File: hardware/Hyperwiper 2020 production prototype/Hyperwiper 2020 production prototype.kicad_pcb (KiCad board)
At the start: 2 copper layers, 87.6 x 59.1 mm, 12 parts, among them K1 Main Power relay, K2 Wiper control relay, Q1 PN2222A, U1 Teensy4.0, U2 Audio board, U3 L7805

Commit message: Updates schematic and PCB boards
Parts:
- added R4: R, Resistor_THT:R_Axial_DIN0207_L6.3mm_D2.5mm_P10.16mm_Horizontal, F.Cu at (972.2, 35.0)
- added R5: R, Resistor_THT:R_Axial_DIN0207_L6.3mm_D2.5mm_P10.16mm_Horizontal, F.Cu at (976.4, 35.0)
- added R6: R, Resistor_THT:R_Axial_DIN0207_L6.3mm_D2.5mm_P10.16mm_Horizontal, F.Cu at (972.2, 48.3)
- added R7: R, Resistor_THT:R_Axial_DIN0207_L6.3mm_D2.5mm_P10.16mm_Horizontal, F.Cu at (976.4, 48.3)
- added R8: R, Resistor_THT:R_Axial_DIN0207_L6.3mm_D2.5mm_P10.16mm_Horizontal, F.Cu at (980.4, 48.3)
- added R9: R, Resistor_THT:R_Axial_DIN0207_L6.3mm_D2.5mm_P10.16mm_Horizontal, F.Cu at (980.4, 35.0)
- moved R1 56.3 mm to (980.4, 11.4), turned to -90 degrees
- moved R2 51.8 mm to (976.4, 21.6), turned to 90 degrees
- moved R3 39.2 mm to (972.2, 21.6), turned to 90 degrees
- moved Q1 18.0 mm to (950.0, 56.5)
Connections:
- D1 pad 1: (no net) -> GND
- D1 pad 2: (no net) -> Net-(D1-Pad2)
- D1 pad 3: (no net) -> Net-(D1-Pad3)
- D1 pad 4: (no net) -> Net-(D1-Pad4)
- D2 pad 1: (no net) -> GND
- D2 pad 2: (no net) -> Net-(D2-Pad2)
- D2 pad 3: (no net) -> Net-(D2-Pad3)
- D2 pad 4: (no net) -> Net-(D2-Pad4)
- D3 pad 1: Net-(D3-Pad1) -> GND
- D3 pad 2: GND -> Net-(D3-Pad2)
- K1 pad 1: (no net) -> Net-(K1-Pad1)
- K2 pad 1: (no net) -> Net-(K1-Pad4)
- K2 pad 3: (no net) -> Net-(K1-Pad1)
- R3 pad 1: Net-(D3-Pad1) -> Net-(D3-Pad2)

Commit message: Update Schematics and PCB
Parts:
- removed R2: R, Resistor_THT:R_Axial_DIN0207_L6.3mm_D2.5mm_P10.16mm_Horizontal
- R1: value R -> 10k
- R3, R4, R5, R6, R7, R8, R9: value R -> 470
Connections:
- R3 pad 2: Net-(K1-Pad3) -> /33

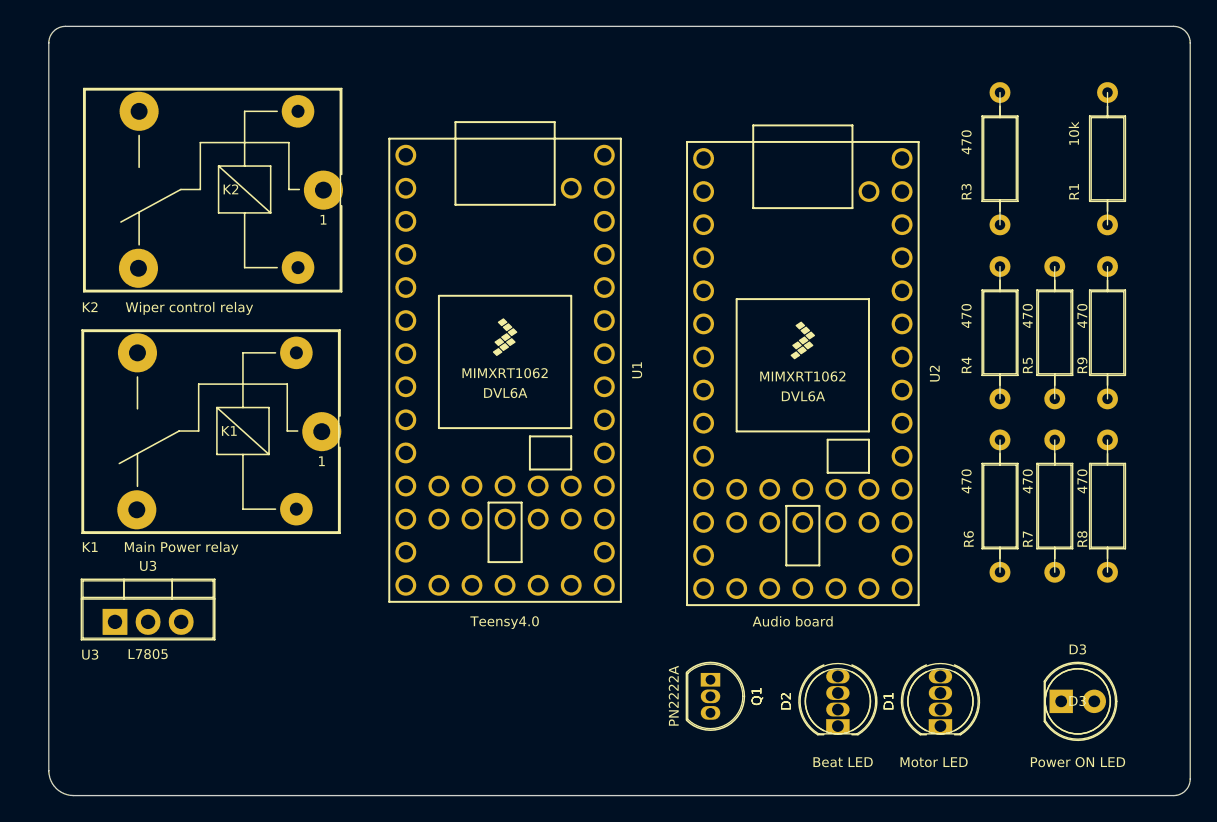
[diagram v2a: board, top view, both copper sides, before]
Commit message: Updated darft schemetics and board.
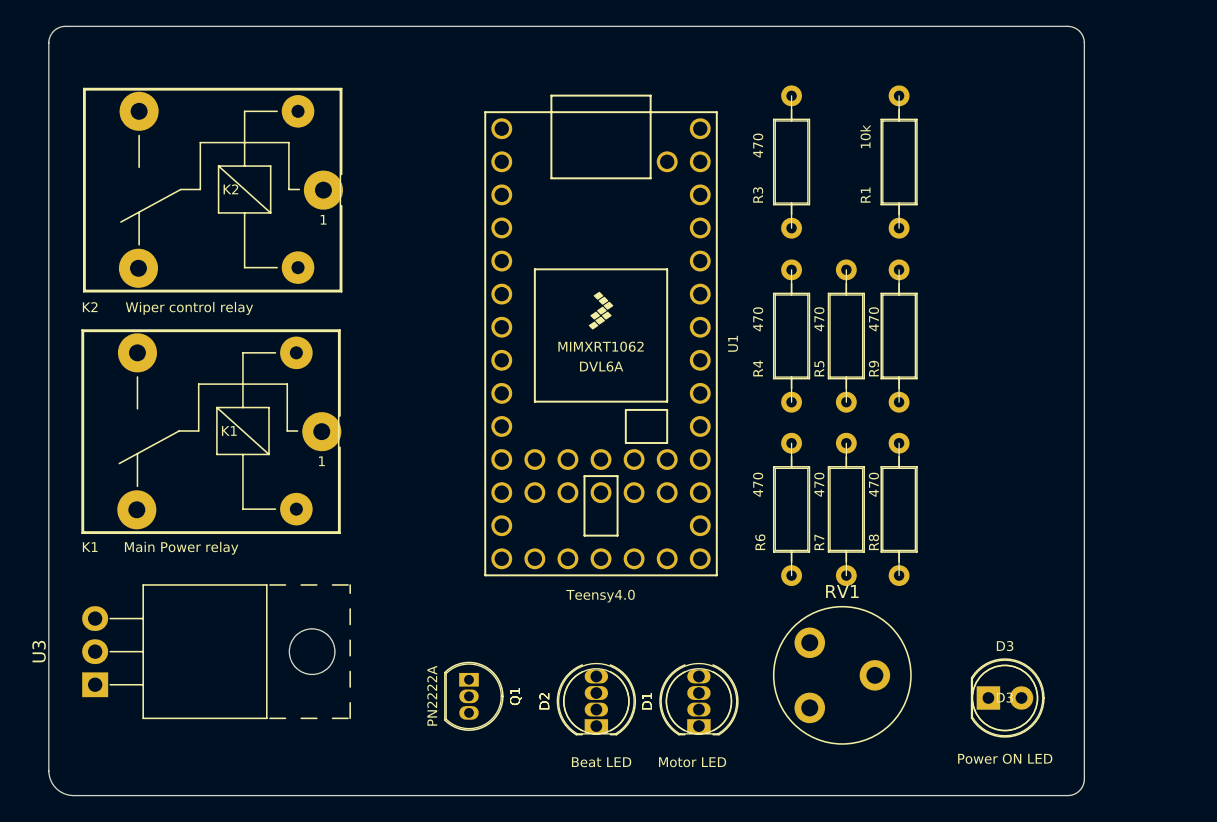
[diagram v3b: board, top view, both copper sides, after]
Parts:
- removed U2: Audio board, Teensy:Teensy40
- added RV1: R_POT_TRIM, Potentiometer_THT:Potentiometer_Piher_PT-10-V05_Vertical, F.Cu at (957.6, 58.7)
- U3: footprint Package_TO_SOT_THT:TO-220-3_Vertical -> Package_TO_SOT_THT:TO-220-3_Horizontal_TabUp
- moved D1 18.5 mm to (949.1, 60.1)
- moved D2 18.5 mm to (941.2, 60.1)
- moved Q1 18.5 mm to (931.4, 56.5)
- moved R1 16.0 mm to (964.4, 11.7)
- moved R8 16.0 mm to (964.4, 48.5)
- moved R9 16.0 mm to (964.4, 35.2)
- moved R3 16.0 mm to (956.2, 21.8)
- moved R4 16.0 mm to (956.2, 35.2)
- moved R5 16.0 mm to (960.4, 35.2)
- moved R6 16.0 mm to (956.2, 48.5)
- moved R7 16.0 mm to (960.4, 48.5)
- moved U1 7.64 mm to (941.6, 30.7)
- moved D3 5.59 mm to (971.3, 57.9)
- moved U3 5.06 mm to (902.7, 56.9), turned to 90 degrees
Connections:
- net /33 renamed /5V
- U1 pad 1: /1 -> (no net)
- U1 pad 10: /10 -> (no net)
- U1 pad 11: /11 -> (no net)
- U1 pad 12: /12 -> (no net)
- U1 pad 13: /13 -> (no net)
- U1 pad 14: /14 -> (no net)
- U1 pad 15: /15 -> (no net)
- U1 pad 16: /16 -> (no net)
- U1 pad 17: /17 -> (no net)
- U1 pad 18: /18 -> (no net)
- U1 pad 19: /19 -> (no net)
- U1 pad 2: /2 -> (no net)
- U1 pad 20: /20 -> (no net)
- U1 pad 21: /21 -> (no net)
- U1 pad 22: /22 -> (no net)
- U1 pad 23: /23 -> (no net)
- U1 pad 24: /24 -> (no net)
- U1 pad 25: /25 -> (no net)
- U1 pad 26: /26 -> (no net)
- U1 pad 27: /27 -> (no net)
- U1 pad 28: /28 -> (no net)
- U1 pad 29: /29 -> (no net)
- U1 pad 3: /3 -> (no net)
- U1 pad 30: /30 -> (no net)
- U1 pad 31: /31 -> (no net)
- U1 pad 32: /32 -> GND
- U1 pad 34: /34 -> (no net)
- U1 pad 4: /4 -> (no net)
- U1 pad 5: /5 -> (no net)
- U1 pad 6: /6 -> (no net)
- U1 pad 7: /7 -> (no net)
- U1 pad 8: /8 -> (no net)
- U1 pad 9: /9 -> (no net)
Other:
- board size 87.6 x 59.1 mm -> 79.5 x 59.1 mm

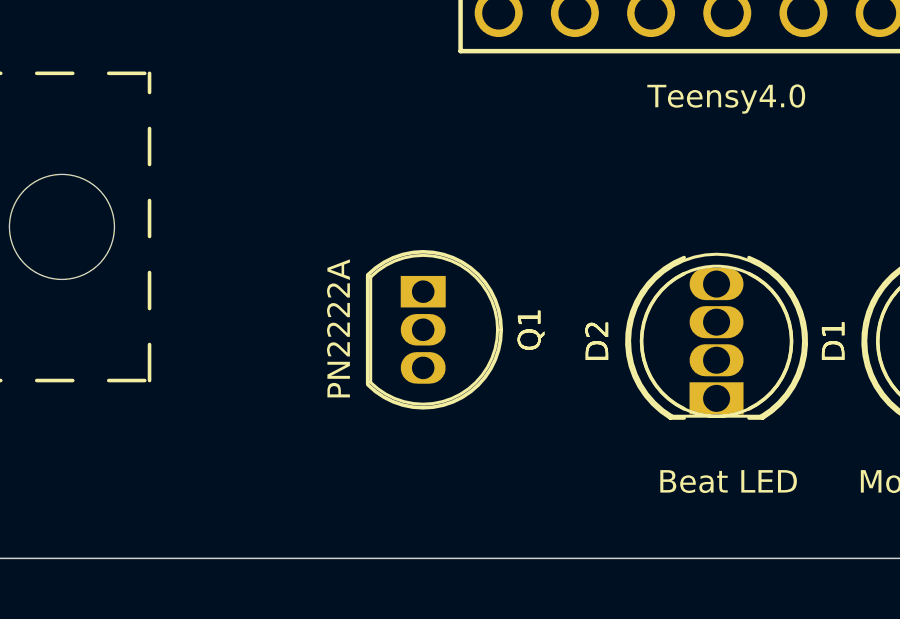
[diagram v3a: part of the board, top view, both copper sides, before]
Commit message: Took out the joystick and display funtions.
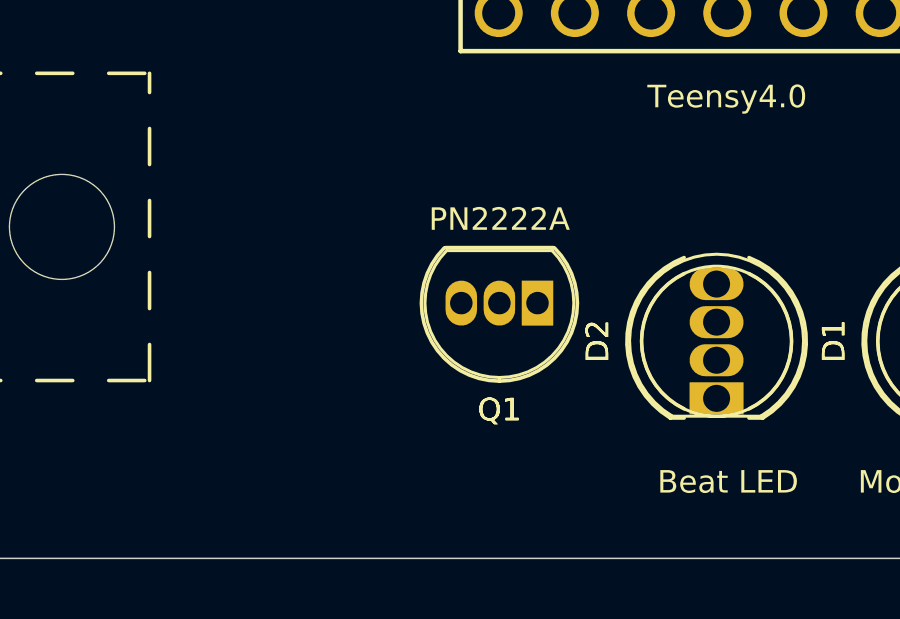
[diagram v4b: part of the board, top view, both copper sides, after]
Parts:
- moved Q1 3.83 mm to (935.2, 56.9), turned to 180 degrees
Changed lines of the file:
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@@
       (net 3 "Net-(K1-Pad3)") (pinfunction "IN"))
     (pad "" np_thru_hole oval (at 2.54 16.66 90) (size 3.5 3.5) (drill 3.5) (layers *.Cu *.Mask))
-    (model "${KISYS3DMOD}/Package_TO_SOT_THT.3dshapes/TO-220-3_Vertical.wrl"
-      (at (xyz 0 0 0))
-      (scale (xyz 1 1 1))
-      (rotate (xyz 0 0 0))
+    (model "${KISYS3DMOD}/Package_TO_SOT_THT.3dshapes/TO-220-3_Horizontal_TabDown.step"
+      (offset (xyz 5 0 0))
+      (scale (xyz 1 1 1))
+      (rotate (xyz 0 0 180))
     )
   )
@@
       (scale (xyz 1 1 1))
       (rotate (xyz 0 0 0))
+    )
+    (model "${KISYS3DMOD}/Potentiometer_THT.3dshapes/Potentiometer_Bourns_3339P_Vertical.step"
+      (offset (xyz 2 5.5 0.5))
+      (scale (xyz 1.2 1.2 1.1))
+      (rotate (xyz 0 0 180))
     )
   )
@@
   )
   (module "Package_TO_SOT_THT:TO-92_Inline" (layer "F.Cu")
-    (at 931.418 56.515 -90)
+    (at 935.228 56.896 180)
     (descr "TO-92 leads in-line, narrow, oval pads, drill 0.75mm (see NXP sot054_po.pdf)")
     (tags "to-92 sc-43 sc-43a sot54 PA33 transistor")
-    (fp_text reference "Q1" (at 1.27 -3.56 90) (layer "F.SilkS")
-      (effects (font (size 0.75 0.75) (thickness 0.15)))
-    )
-    (fp_text value "PN2222A" (at 1.27 2.79 90 unlocked) (layer "F.SilkS")
+    (fp_text reference "Q1" (at 1.27 -3.56) (layer "F.SilkS")
+      (effects (font (size 0.75 0.75) (thickness 0.15)))
+    )
+    (fp_text value "PN2222A" (at 1.27 2.79 unlocked) (layer "F.SilkS")
       (effects (font (size 0.75 0.75) (thickness 0.15)))
     )
@@
     (fp_line (start -0.5 1.75) (end 3 1.75) (layer "F.SilkS") (width 0.1))
     (fp_line (start -0.53 1.85) (end 3.07 1.85) (layer "F.SilkS") (width 0.12))
-    (fp_text user "${REFERENCE}" (at 1.27 -3.56 90 unlocked) (layer "F.SilkS")
-      (effects (font (size 0.75 0.75) (thickness 0.15)))
-    )
-    (pad "1" thru_hole rect (at 0 0 270) (size 1.05 1.5) (drill 0.75) (layers *.Cu *.Mask)
+    (fp_text user "${REFERENCE}" (at 1.27 -3.56 unlocked) (layer "F.SilkS")
+      (effects (font (size 0.75 0.75) (thickness 0.15)))
+    )
+    (pad "1" thru_hole rect (at 0 0 180) (size 1.05 1.5) (drill 0.75) (layers *.Cu *.Mask)
       (net 5 "GND") (pinfunction "E"))
-    (pad "3" thru_hole oval (at 2.54 0 270) (size 1.05 1.5) (drill 0.75) (layers *.Cu *.Mask)
+    (pad "3" thru_hole oval (at 2.54 0 180) (size 1.05 1.5) (drill 0.75) (layers *.Cu *.Mask)
       (net 4 "Net-(K2-Pad2)") (pinfunction "C"))
-    (pad "2" thru_hole oval (at 1.27 0 270) (size 1.05 1.5) (drill 0.75) (layers *.Cu *.Mask)
+    (pad "2" thru_hole oval (at 1.27 0 180) (size 1.05 1.5) (drill 0.75) (layers *.Cu *.Mask)
       (net 6 "Net-(Q1-Pad2)") (pinfunction "B"))
     (model "${KISYS3DMOD}/Package_TO_SOT_THT.3dshapes/TO-92_Inline.wrl"

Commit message: Updated Schematic and board.
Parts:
- added X1: W237-3E-bGeigieNanoKit_V1.1r5a-eagle-import, DWP 2020:W237-3E, F.Cu at (910.3, 55.9)
- added X2: W237-3E-bGeigieNanoKit_V1.1r5a-eagle-import, DWP 2020:W237-3E, F.Cu at (926.7, 55.9)
- U3: footprint Package_TO_SOT_THT:TO-220-3_Horizontal_TabUp -> Package_TO_SOT_THT:TO-220-3_Vertical
- moved U3 20.9 mm to (904.0, 36.1)
- moved R3 20.1 mm to (975.4, 15.9), turned to 180 degrees
- moved U1 11.0 mm to (952.2, 27.9)
- moved R4 10.3 mm to (966.1, 32.4)
- moved R6 10.3 mm to (966.1, 45.7)
- moved R8 10.3 mm to (974.3, 45.7)
- moved R9 10.3 mm to (974.3, 32.4)
- moved R5 10.3 mm to (970.3, 32.4)
- moved R7 10.3 mm to (970.3, 45.7)
- moved D1 7.20 mm to (953.8, 54.6)
- moved D2 7.20 mm to (945.9, 54.6)
- moved Q1 7.01 mm to (940.1, 51.8)
- moved K1 6.23 mm to (926.2, 36.2)
- moved K2 6.23 mm to (926.3, 17.7)
- moved D3 4.85 mm to (971.8, 53.1)
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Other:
- board size 79.5 x 59.1 mm -> 79.5 x 57.3 mm
